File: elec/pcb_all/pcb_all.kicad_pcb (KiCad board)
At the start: 2 copper layers, 59.2 x 116.5 mm, 80 parts, among them IC1 TPS629203QDRLRQ1, IC2 AP63203WU-7, IC3 BQ25176MDSGR, IC4 TPS61023DRLR, IC5 BMP390, IC6 LSM6DSLTR, J1 Conn_01x02, J2 Conn_01x07, Q1 CSD16301Q2, Q2 CSD16301Q2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

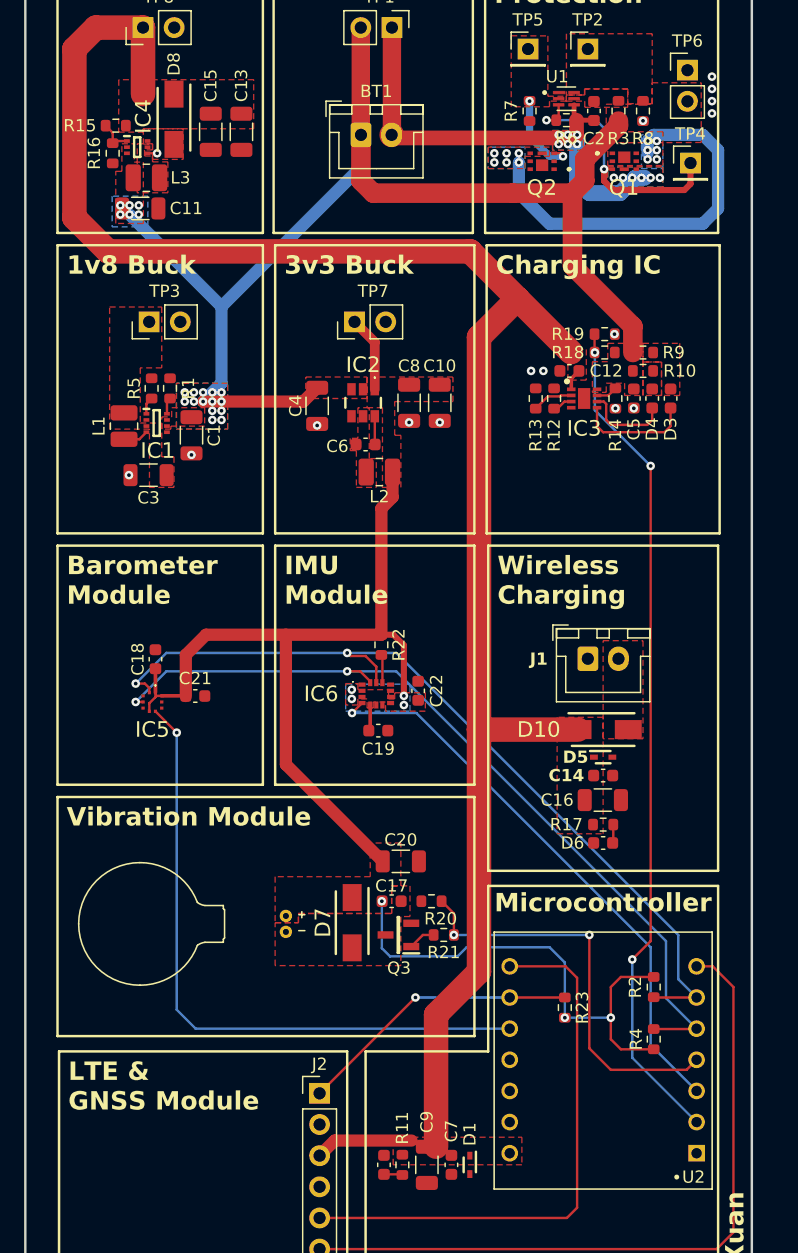
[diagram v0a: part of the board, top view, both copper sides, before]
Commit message: completed most jlc part numbers, pending reduce number of extended & find replacement for 1v8 buck
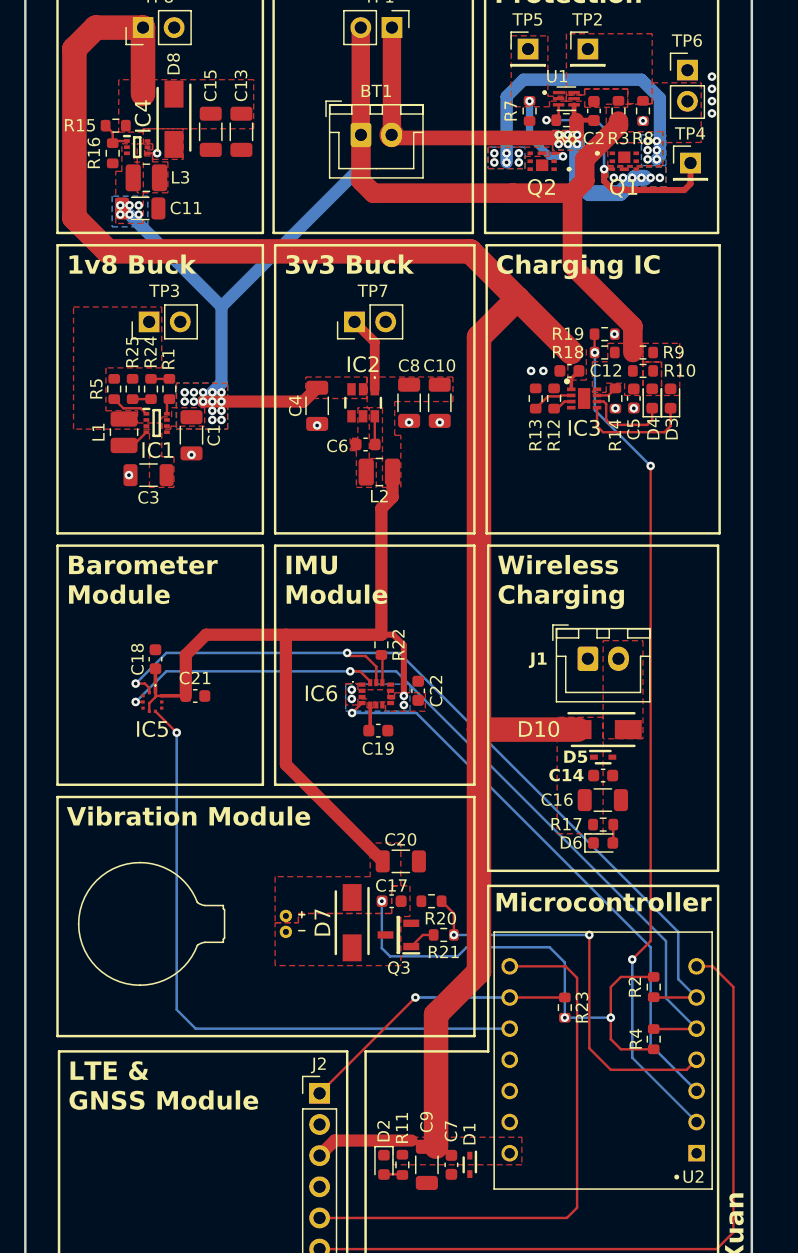
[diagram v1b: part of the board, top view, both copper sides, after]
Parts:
- added R24: 2k, Resistor_SMD:R_0603_1608Metric, F.Cu at (125.0, 89.2)
- added R25: 2k, Resistor_SMD:R_0603_1608Metric, F.Cu at (123.5, 89.2)
- C17, C2: value 0.1uF -> 100nF
- D2, D3, D4, D6: footprint Capacitor_SMD:C_0603_1608Metric -> LED_SMD:LED_0603_1608Metric
- R1: value 34k -> 30k
- R13: value 604 -> 604R
- moved R5 3.05 mm to (122.0, 89.2)
- moved L1 0.50 mm to (122.8, 92.8)
- moved R1 0.07 mm to (126.5, 89.2)
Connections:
- R1 pad 2: GND -> Net-(R1-Pad2)
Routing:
- net Net-(Q1-D): track 32.5 -> 24.2 mm
- net Net-(IC1-FB/VSET): track 1.43 -> 3.12 mm
- net Net-(R24-Pad1): track 0.00 -> 1.50 mm
- net Net-(R1-Pad2): track 0.00 -> 1.50 mm

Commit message: did stuff
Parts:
- added R26: 30k, Resistor_SMD:R_0603_1608Metric, F.Cu at (120.5, 89.2)
- added R27: 4.7k, Resistor_SMD:R_0603_1608Metric, F.Cu at (119.0, 89.2)
- R15: value 732k -> 68k
- R16: value 100k -> 510k
- R5: value 64.9k -> 30k
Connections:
- R5 pad 2: GND -> Net-(R26-Pad2)
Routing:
- net Net-(R26-Pad2): track 0.00 -> 1.50 mm
- net Net-(R26-Pad1): track 0.00 -> 1.50 mm
- net GND: vias 16 -> 18
